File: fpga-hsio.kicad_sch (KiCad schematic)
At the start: 3 parts, among them U1 MPFS250T-FCVG484, Y5 Oscillator_50MHz_ECS_1612MV

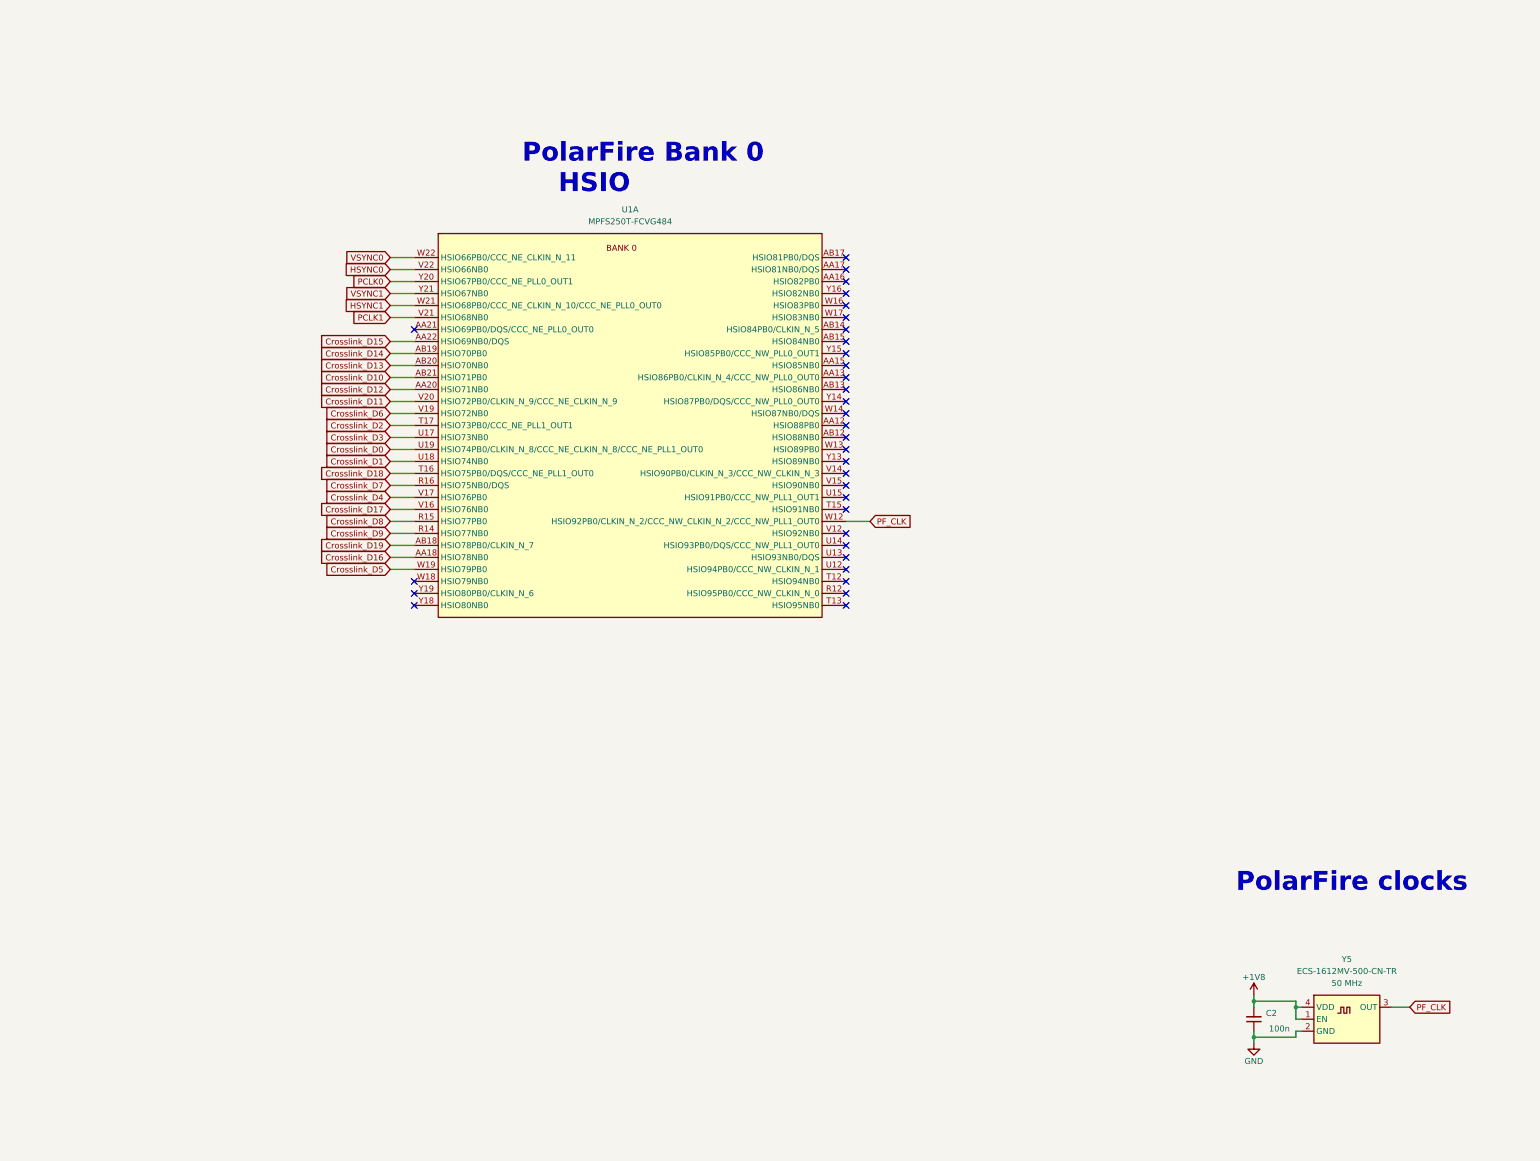
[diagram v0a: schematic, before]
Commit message: [#57505] Continue migration to hierarchical schematic
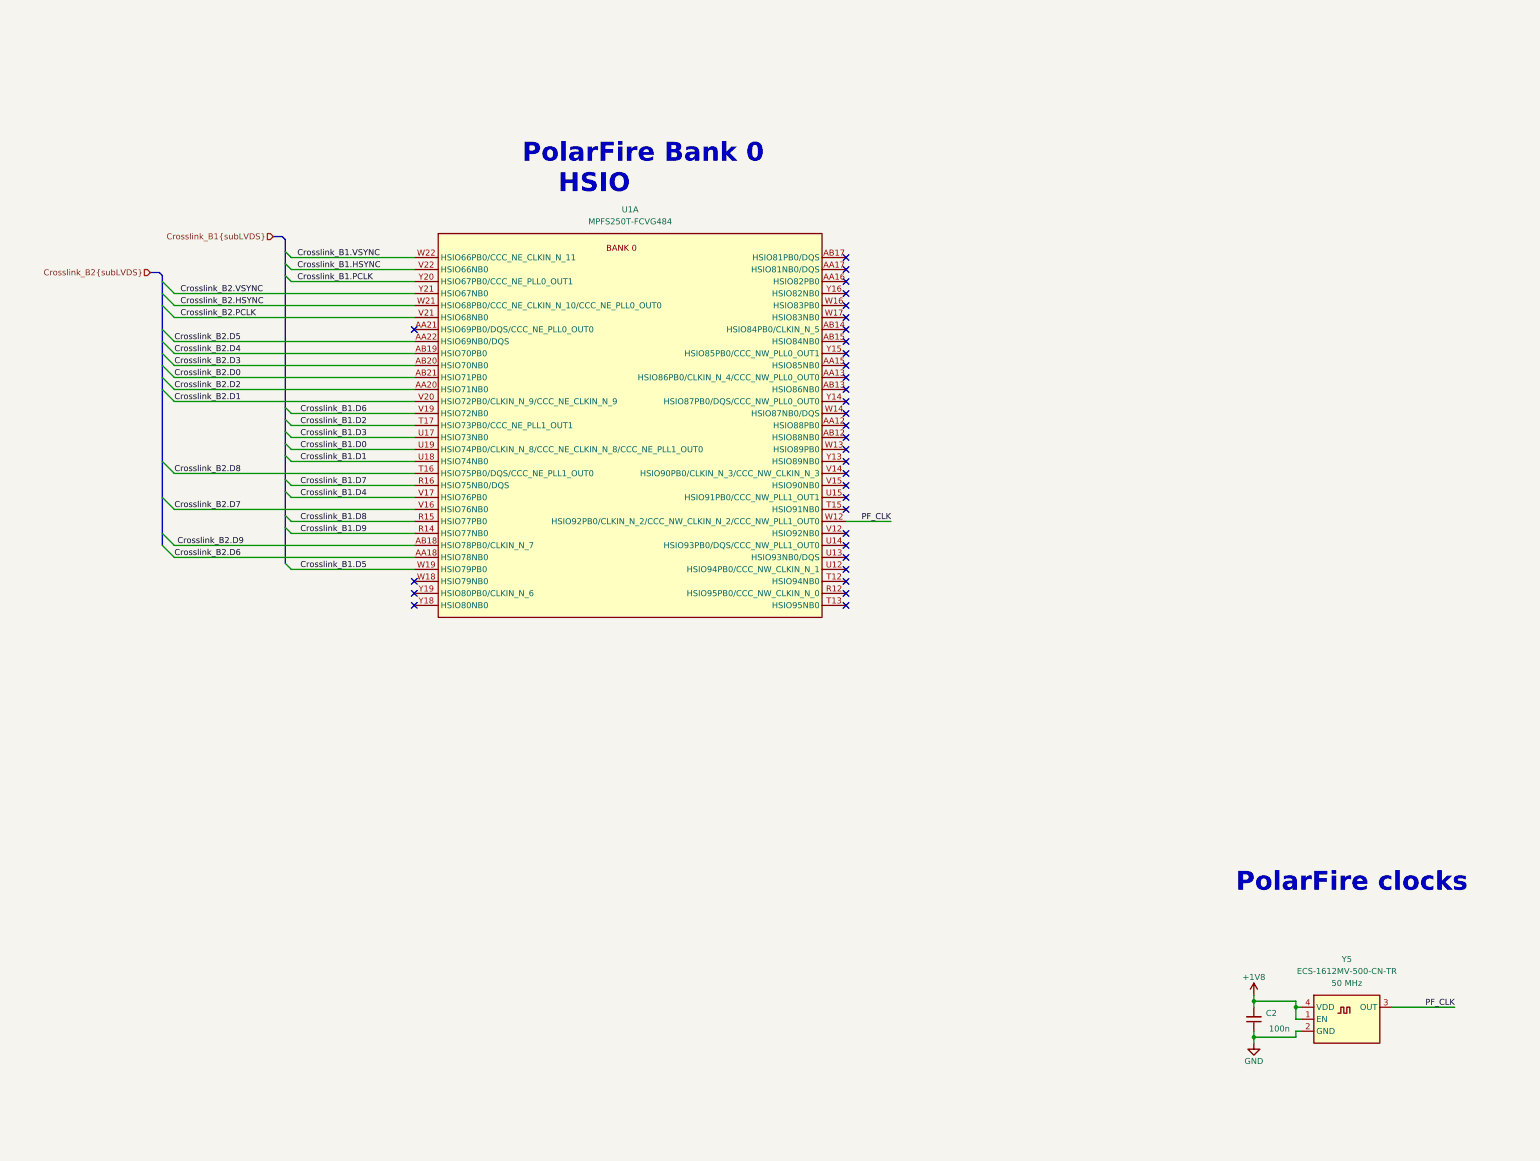
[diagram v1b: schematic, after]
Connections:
- net Crosslink_D0 renamed Crosslink_B1.D0
- net Crosslink_D1 renamed Crosslink_B1.D1
- net Crosslink_D10 renamed Crosslink_B2.D0
- net Crosslink_D11 renamed Crosslink_B2.D1
- net Crosslink_D12 renamed Crosslink_B2.D2
- net Crosslink_D13 renamed Crosslink_B2.D3
- net Crosslink_D14 renamed Crosslink_B2.D4
- net Crosslink_D15 renamed Crosslink_B2.D5
- net Crosslink_D16 renamed Crosslink_B2.D6
- net Crosslink_D17 renamed Crosslink_B2.D7
- net Crosslink_D18 renamed Crosslink_B2.D8
- net Crosslink_D19 renamed Crosslink_B2.D9
- net Crosslink_D2 renamed Crosslink_B1.D2
- net Crosslink_D3 renamed Crosslink_B1.D3
- net Crosslink_D4 renamed Crosslink_B1.D4
- net Crosslink_D5 renamed Crosslink_B1.D5
- net Crosslink_D6 renamed Crosslink_B1.D6
- net Crosslink_D7 renamed Crosslink_B1.D7
- net Crosslink_D8 renamed Crosslink_B1.D8
- net Crosslink_D9 renamed Crosslink_B1.D9
- net HSYNC0 renamed Crosslink_B1.HSYNC
- net HSYNC1 renamed Crosslink_B2.HSYNC
- net PCLK0 renamed Crosslink_B1.PCLK
- net PCLK1 renamed Crosslink_B2.PCLK
- net VSYNC0 renamed Crosslink_B1.VSYNC
- net VSYNC1 renamed Crosslink_B2.VSYNC

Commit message: [#57422] Finishing touches
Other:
- note added: "PolarFire main clock"
- note removed: "PolarFire clocks"
- moved on the sheet: C2, U1A, Y5

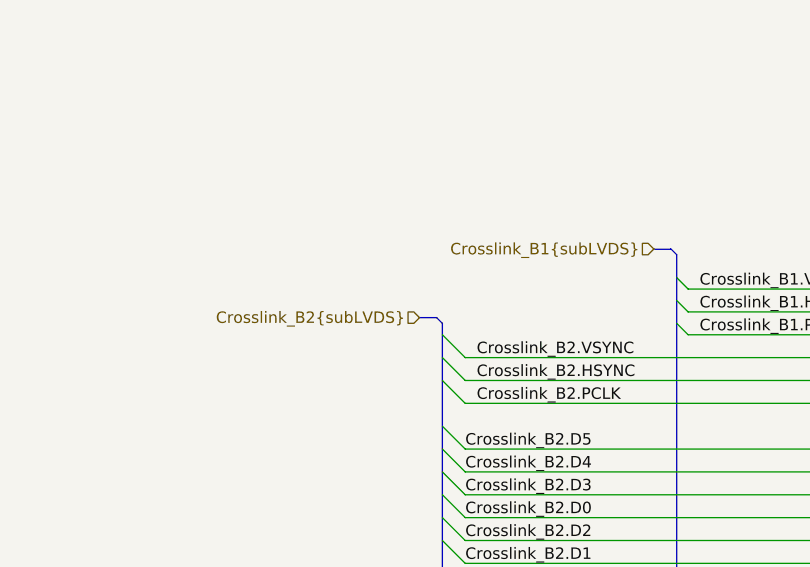
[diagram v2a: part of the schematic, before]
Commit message: [#57878] Fix power planes and bus naming
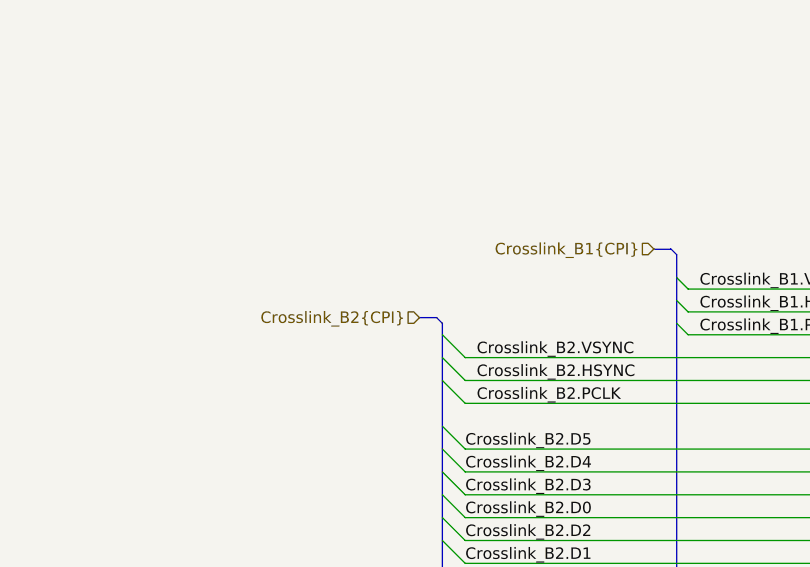
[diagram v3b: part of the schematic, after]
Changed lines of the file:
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@@
     (effects (font (size 1.27 1.27)) (justify left bottom))
   )
-  (hierarchical_label "Crosslink_B1{subLVDS}" (shape input) (at 149.225 71.755 180) (fields_autoplaced)
+  (hierarchical_label "Crosslink_B1{CPI}" (shape input) (at 149.225 71.755 180) (fields_autoplaced)
     (effects (font (size 1.27 1.27)) (justify right))
   )
-  (hierarchical_label "Crosslink_B2{subLVDS}" (shape input) (at 123.19 79.375 180) (fields_autoplaced)
+  (hierarchical_label "Crosslink_B2{CPI}" (shape input) (at 123.19 79.375 180) (fields_autoplaced)
     (effects (font (size 1.27 1.27)) (justify right))
   )

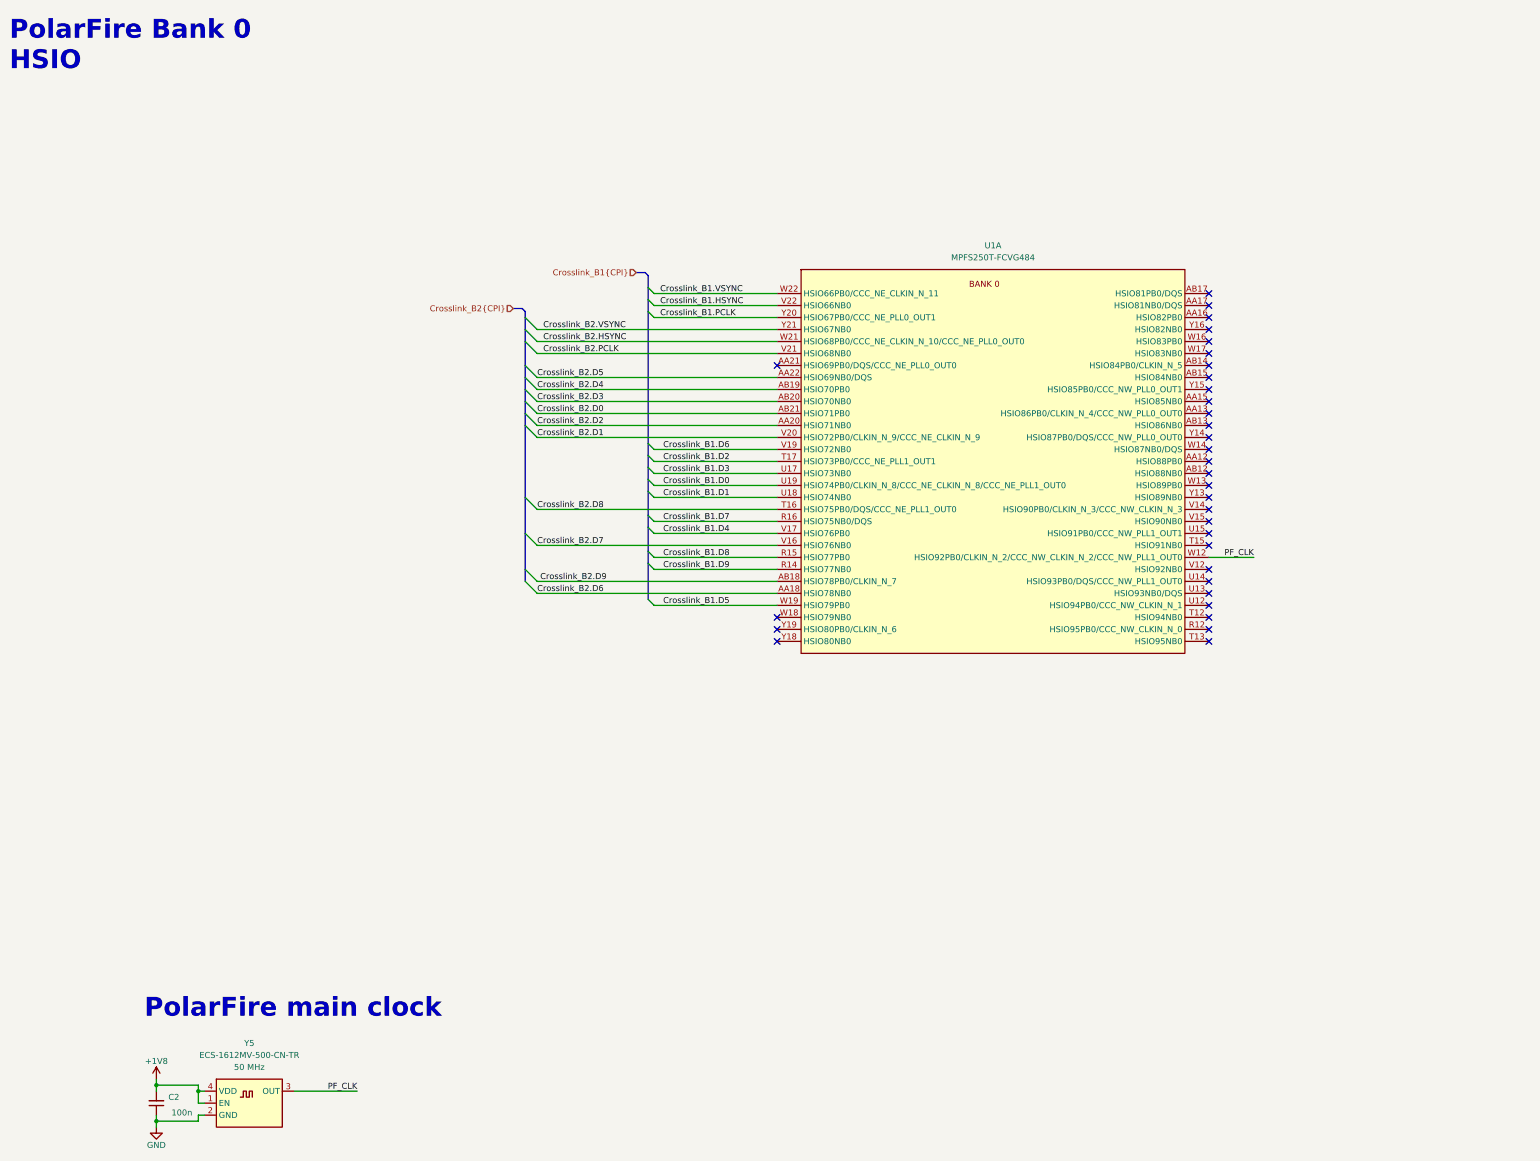
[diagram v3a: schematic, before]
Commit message: [#57422] Align schematics
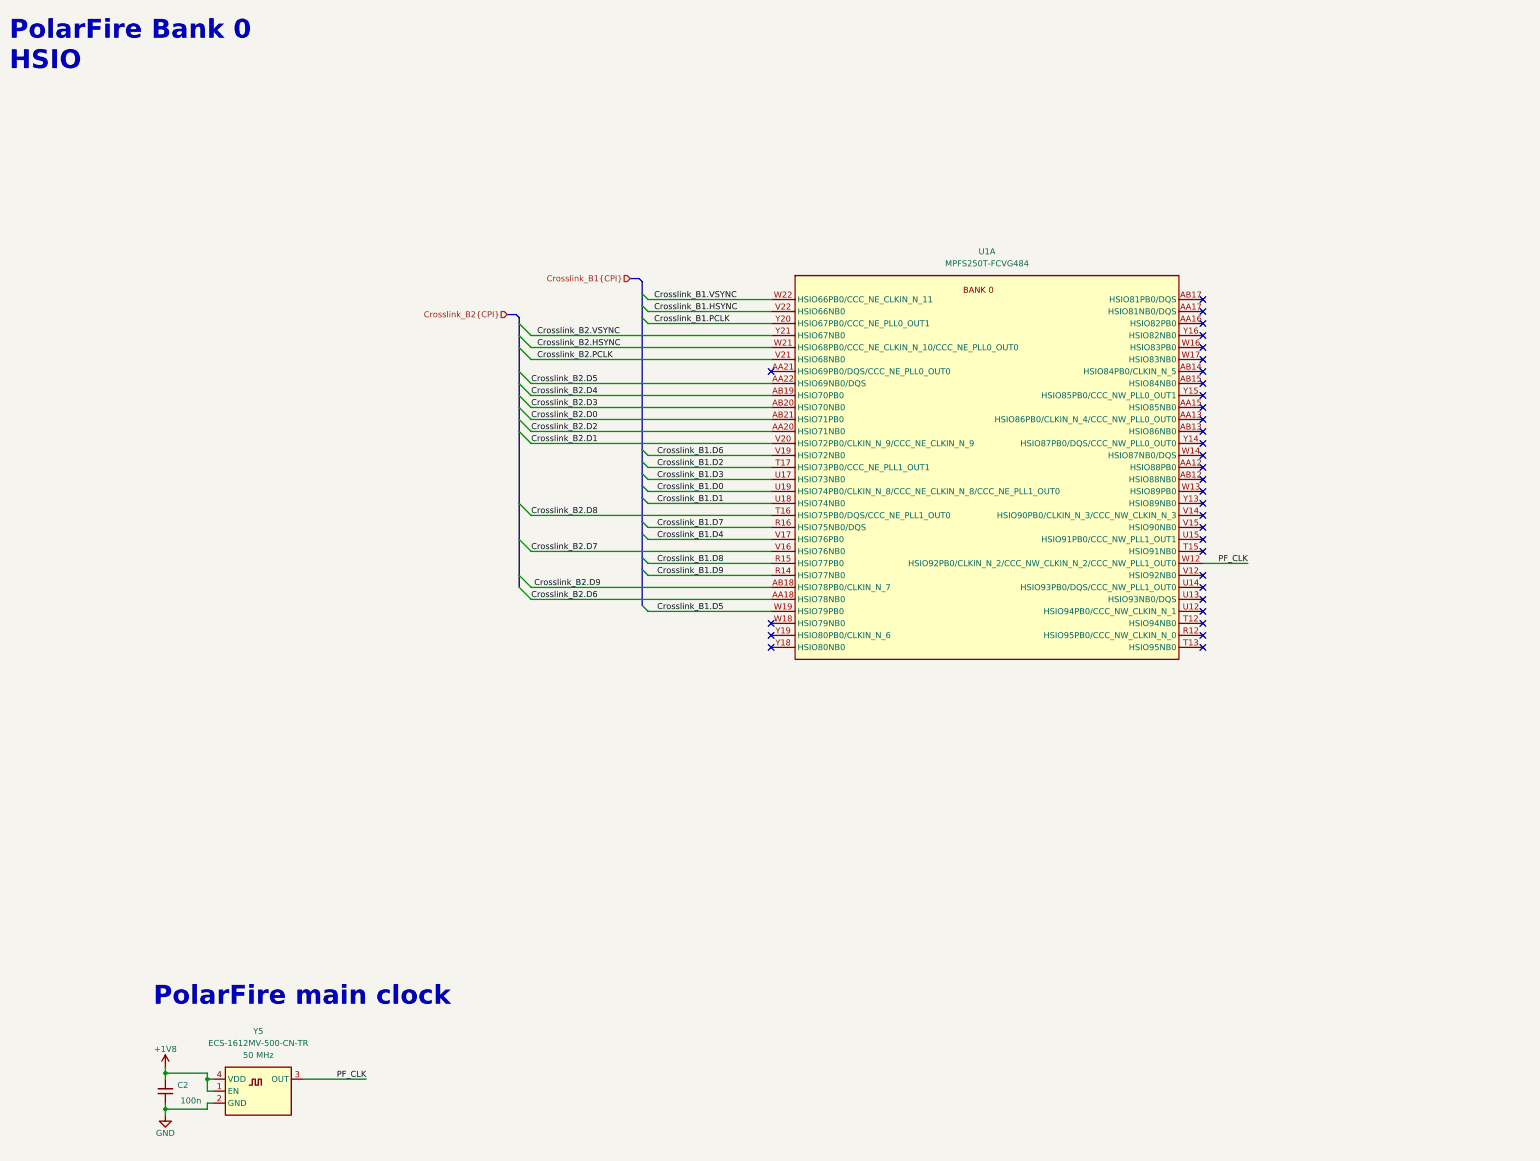
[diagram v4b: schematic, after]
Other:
- moved on the sheet: C2, U1A, Y5
